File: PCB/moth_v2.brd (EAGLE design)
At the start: 94 x 94 mm, 86 parts, among them Q1 PNO8l07

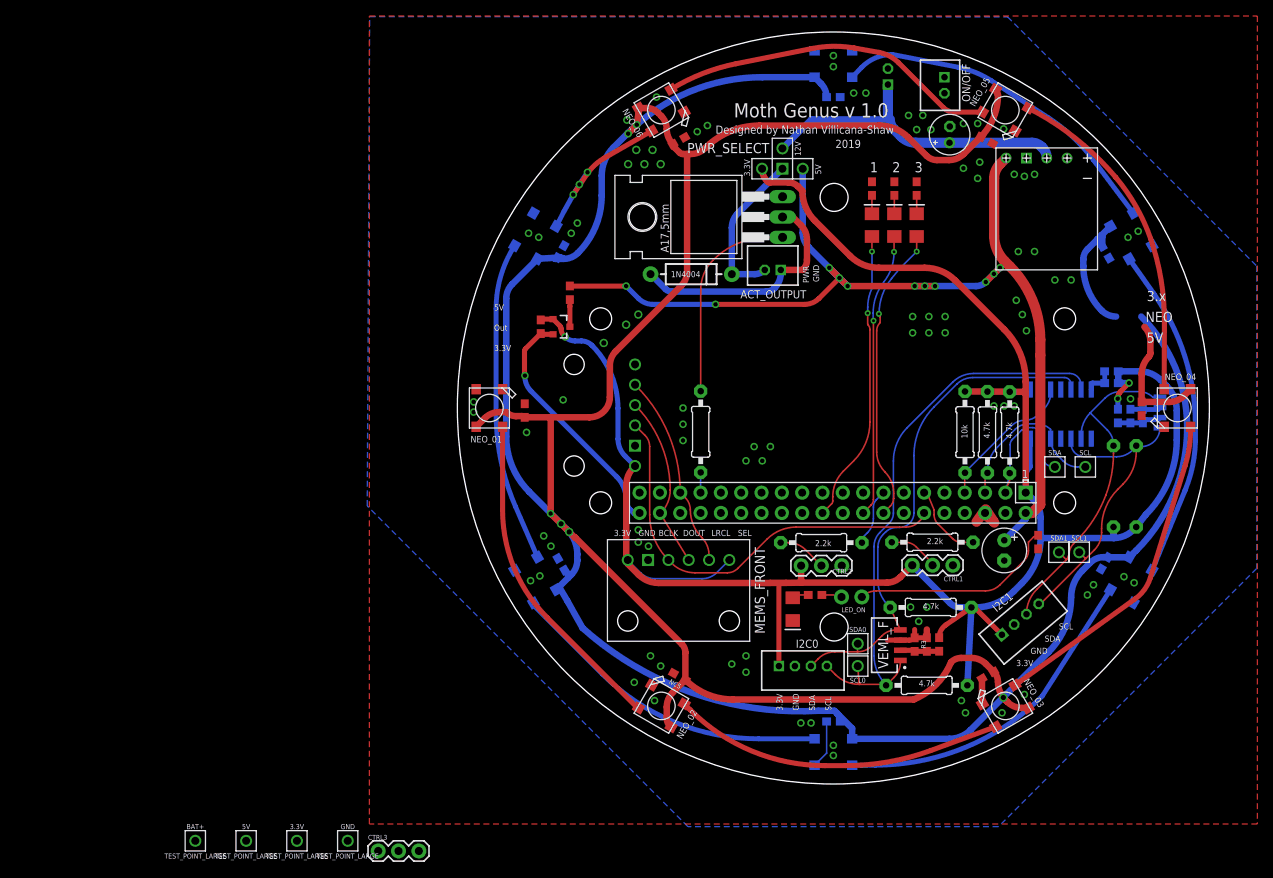
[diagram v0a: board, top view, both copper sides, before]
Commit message: got a working version of the VEML sensors working through the TCA9543A
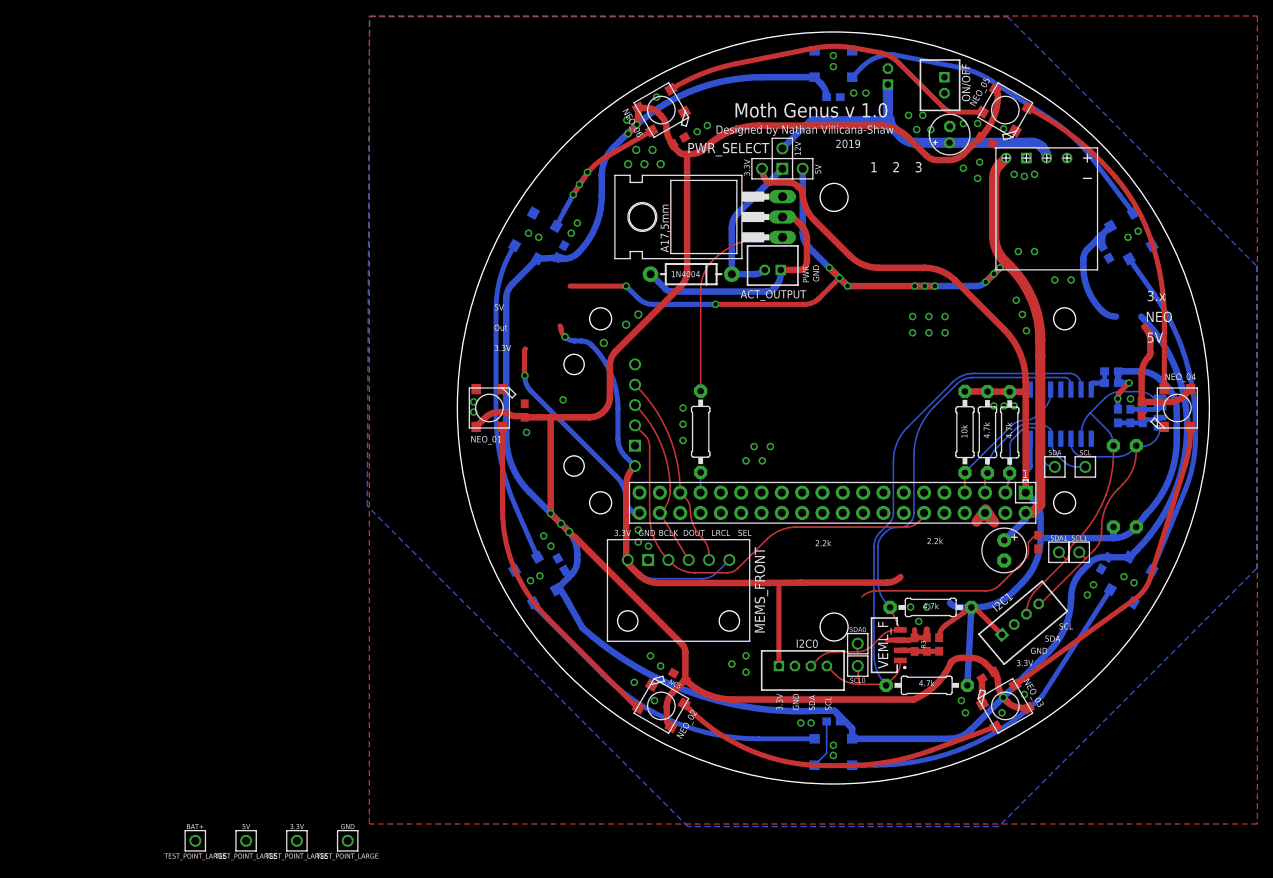
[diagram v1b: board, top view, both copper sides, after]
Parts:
- removed CTRL1, CTRL2, CTRL3: (no value), SparkFun-Connectors:1X03
- removed D2, D3, D5, D6: (no value), SparkFun-LED:FKIT-LED-1206
- removed LED_ON: (no value), SparkFun-Connectors:1X02_NO_SILK
- removed R10, R11, R17, R18: 4.7k, SparkFun-Resistors:0603
- removed R12, R14: 2k, adafruit:0207/10
- removed R15, R16: 10k, SparkFun-Resistors:0603
- removed U$2: BSS138, nathans-custom-parts:SOT23-3
- C1, C15, C2, C21: value 100nf -> 0.1uf
- NC1, NC10, NC11, NC12, NC2, NC3, NC4, NC5, NC6, NC7, NC8, NC9: value 1uf -> 0.1uf
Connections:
- removed net N$15: R14.1, U$3.15
- removed net N$16: D2.A, R10.2
- removed net N$17: CTRL2.2, R14.2
- removed net N$18: CTRL1.2, R12.2
- removed net N$27: LED_ON.1, R10.1
- removed net N$28: D3.C, R11.2
- removed net N$29: D5.C, R17.2
- removed net N$3: R12.1, U$3.11
- removed net N$30: D6.C, R18.2
- removed net N$32: D3.A, U$3.16
- removed net N$33: D5.A, U$3.18
- removed net N$34: D6.A, U$3.22
- net 3.3V: no longer CTRL1.3, CTRL2.3, R16.1, U$2.1
- net 5V: no longer CTRL3.1, LED_ON.2, R15.2
- net GND: no longer CTRL1.1, CTRL2.1, CTRL3.3, D2.C, R11.1, R17.1, R18.1
- net NEO_P: no longer R16.2, U$2.2
- net NEO_P_CTRL: no longer CTRL3.2, R15.1, U$2.3
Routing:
- net N$32: track 37.1 -> 0.00 mm, vias 2 -> 0
- net N$34: track 36.4 -> 0.00 mm, vias 2 -> 0
- net N$33: track 35.5 -> 0.00 mm, vias 2 -> 0
- net 3.3V: track 273.1 -> 259.4 mm
- net N$3: track 9.63 -> 0.00 mm
- net N$15: track 7.09 -> 0.00 mm
- net N$18: track 6.31 -> 0.00 mm
- net N$17: track 6.10 -> 0.00 mm
- net NEO_P: track 30.7 -> 26.5 mm
- net NEO_P_CTRL: track 3.39 -> 0.00 mm
- net N$27: track 2.50 -> 0.00 mm
- net N$30: track 2.30 -> 0.00 mm
- net N$29: track 2.30 -> 0.00 mm
- net N$28: track 2.30 -> 0.00 mm
- net N$16: track 2.21 -> 0.00 mm

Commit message: new but untested auto_gain control also minor updates to the v2 PCB
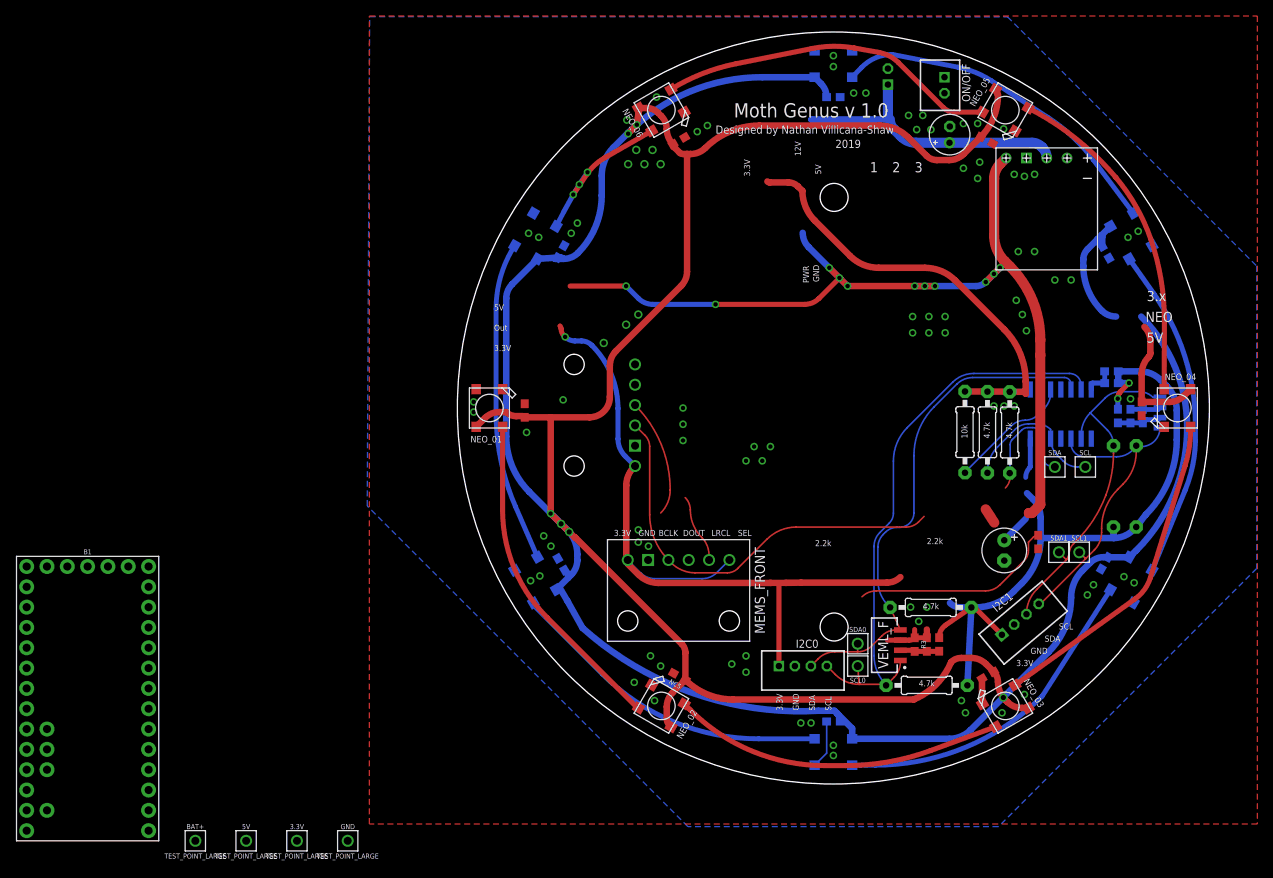
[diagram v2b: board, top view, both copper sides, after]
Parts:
- removed ACT_OUTPUT: B2B-PH-K, con-jst-ph:B2B-PH-K
- removed D4: 1N4004, SparkFun-DiscreteSemi:DIODE-1N4001
- removed Q1: PNO8l07, transistor-power:TO220BH
- removed R13: 660R, adafruit:0207/10
- removed U$3: RPI-ZERO, RPI-Zero:RASPBERRYPI_BASTELSTUBE_V13_RASPI_BOARD_B+_FULL
- removed U$7: PWR_SELECT, nathans-custom-parts:PWR_SELECT_PINOUT
- added B1: TEENSY-3.1NOSILK, SparkFun-Boards:TEENSY-3.1_NOSILK
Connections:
- removed net N$19: Q1.G, R13.2
- removed net N$20: ACT_OUTPUT.1, D4.A, Q1.D
- removed net NEO_P: U$3.40
- removed net S-PWR: ACT_OUTPUT.2, D4.C, U$7.IN
- removed net SOL1: R13.1, U$3.33
- new net 3V: B1.3V
- new net AGND: B1.AGND
- new net GND1: B1.GND1
- new net VBAT: B1.VBAT
- new net VIN: B1.VIN
- new net VUSB: B1.VUSB
- net 3.3V: now also B1.3.3V; no longer U$3.1, U$7.3.3V
- net 5V: no longer U$3.2, U$7.5V
- net BAT_IN: no longer U$7.12V
- net BCLK: no longer U$3.12
- net GND: now also B1.GND; no longer Q1.S, U$3.6
- net I2C_RESET: no longer U$3.7
- net I2S_DATA: no longer U$3.38
- net LRCLK: no longer U$3.35
- net SCL: now also B1.19; no longer U$3.5
- net SDA: now also B1.18; no longer U$3.3
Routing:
- net N$20: track 30.2 -> 0.00 mm
- net NEO_P: track 26.5 -> 0.00 mm, vias 1 -> 0
- net N$19: track 25.9 -> 0.00 mm
- net S-PWR: track 19.9 -> 0.00 mm
- net 3.3V: track 259.4 -> 243.3 mm
- net LRCLK: track 23.9 -> 8.55 mm
- net 5V: track 623.2 -> 614.1 mm
- net I2S_DATA: track 21.6 -> 14.6 mm
- net BAT_IN: track 41.3 -> 36.2 mm
- net GND: track 29.5 -> 26.0 mm
- net SDA: track 20.0 -> 16.9 mm
- net SOL1: track 2.53 -> 0.00 mm
- net I2C_RESET: track 18.0 -> 15.6 mm
- net SCL: track 21.2 -> 19.1 mm
